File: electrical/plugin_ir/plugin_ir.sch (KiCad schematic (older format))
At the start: 2 parts, among them Q2 AO3400

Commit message: Merge from master
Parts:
- renumbered Q2 to Q?, R4 to R?
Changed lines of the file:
@@
 EESchema Schematic File Version 4
-LIBS:rasbot-cache
 EELAYER 29 0
 EELAYER END
 $Descr A4 11693 8268
 encoding utf-8
-Sheet 4 14
+Sheet 1 8
 Title ""
 Date ""
@@
 IR_OUT6
 $Comp
-L power:GND #PWR031
+L power:GND #PWR?
 U 1 1 5D41F6C3
 P 5300 7250
-F 0 "#PWR031" H 5300 7000 50  0001 C CNN
+F 0 "#PWR?" H 5300 7000 50  0001 C CNN
 F 1 "GND" H 5305 7077 50  0000 C CNN
 F 2 "" H 5300 7250 50  0001 C CNN
@@
 	5300 6750 5300 6700
 $Comp
-L Device:R R4
+L Device:R R?
 U 1 1 5D3ABC64
 P 5850 6950
-F 0 "R4" H 5920 6996 50  0000 L CNN
+F 0 "R?" H 5920 6996 50  0000 L CNN
 F 1 "0" H 5920 6905 50  0000 L CNN
 F 2 "Resistor_SMD:R_0805_2012Metric" V 5780 6950 50  0001 C CNN
@@
 	4950 1000 4950 6150
 $Comp
-L rasbot:AO3400 Q2
+L rasbot:AO3400 Q?
 U 1 1 5D3E0C2F
 P 5150 6950
-F 0 "Q2" H 5406 6996 50  0000 L CNN
+F 0 "Q?" H 5406 6996 50  0000 L CNN
 F 1 "AO3400" H 5406 6905 50  0000 L CNN
 F 2 "Package_TO_SOT_SMD:SOT-23" H 5975 6875 50  0001 C CNN

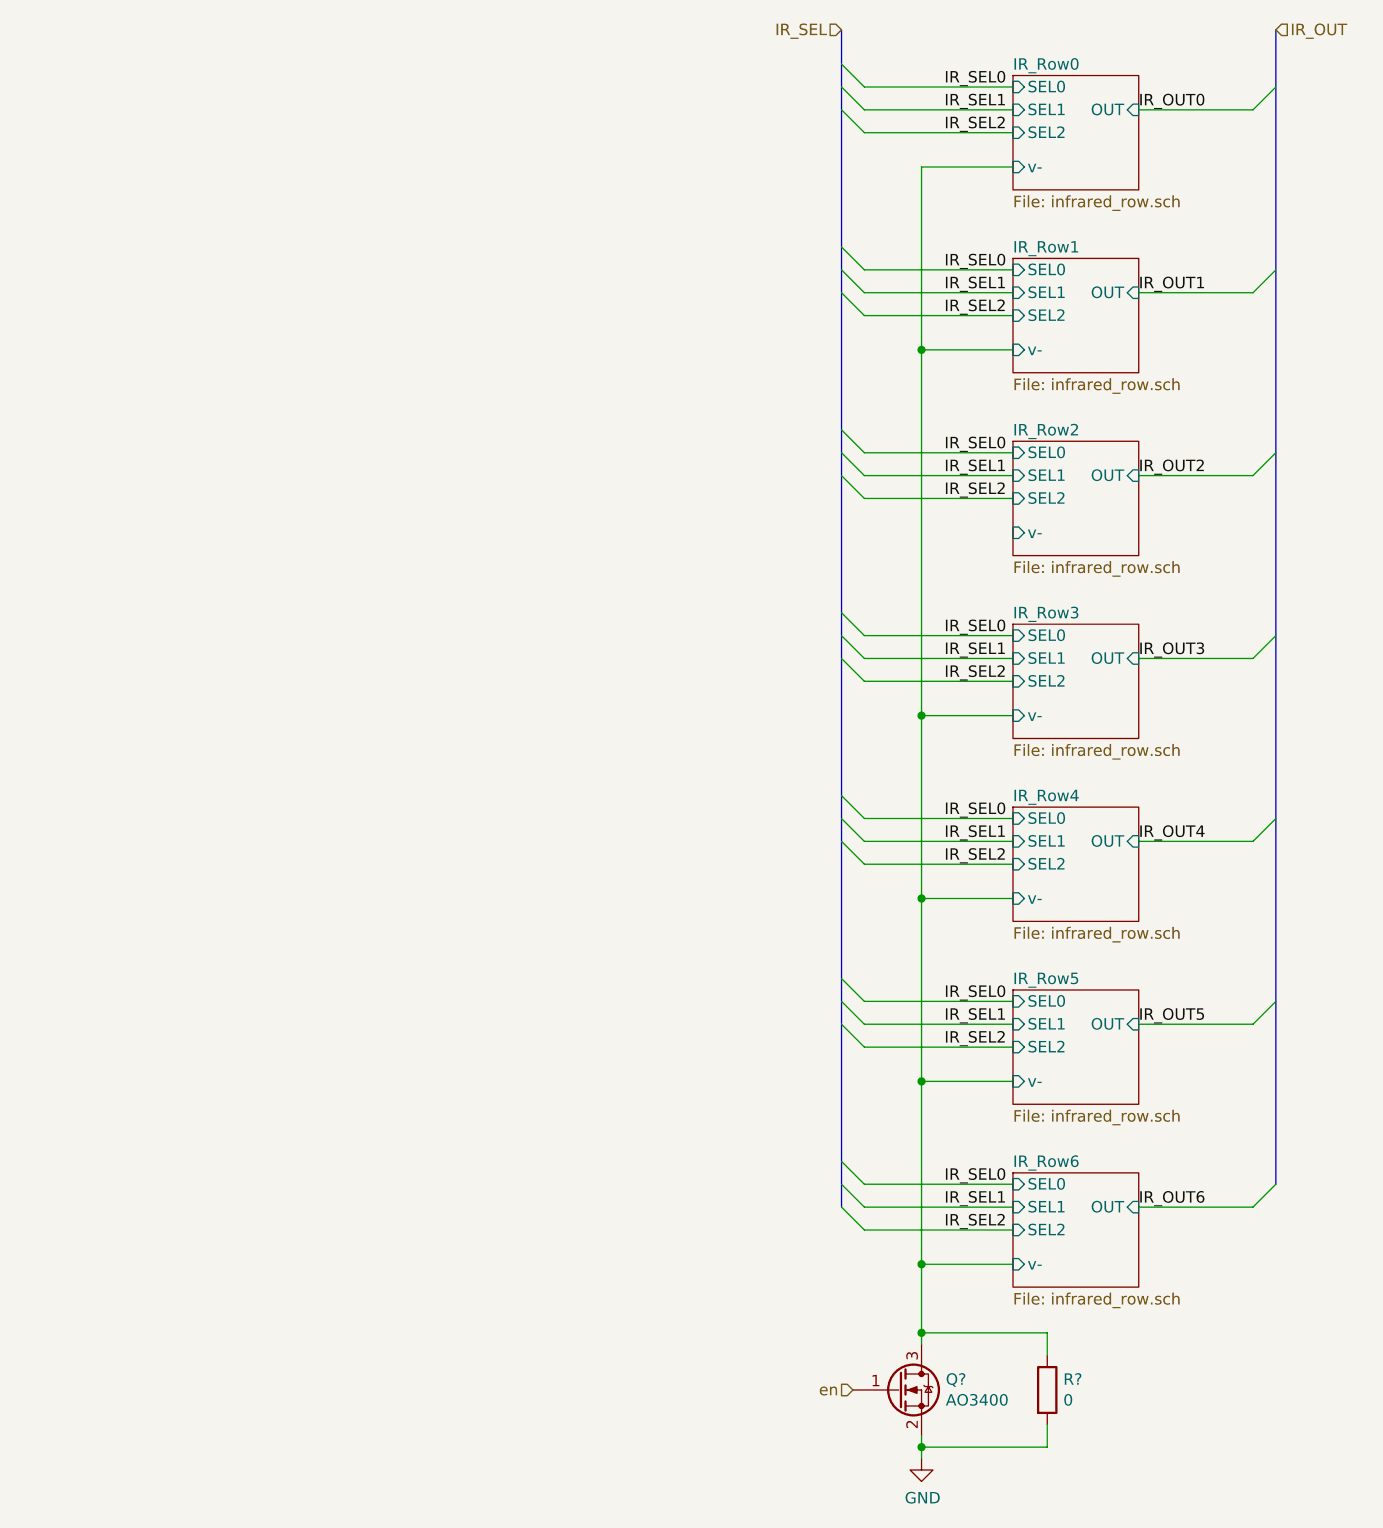
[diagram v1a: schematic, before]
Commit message: Give Up SEPIC and 9V LDO design
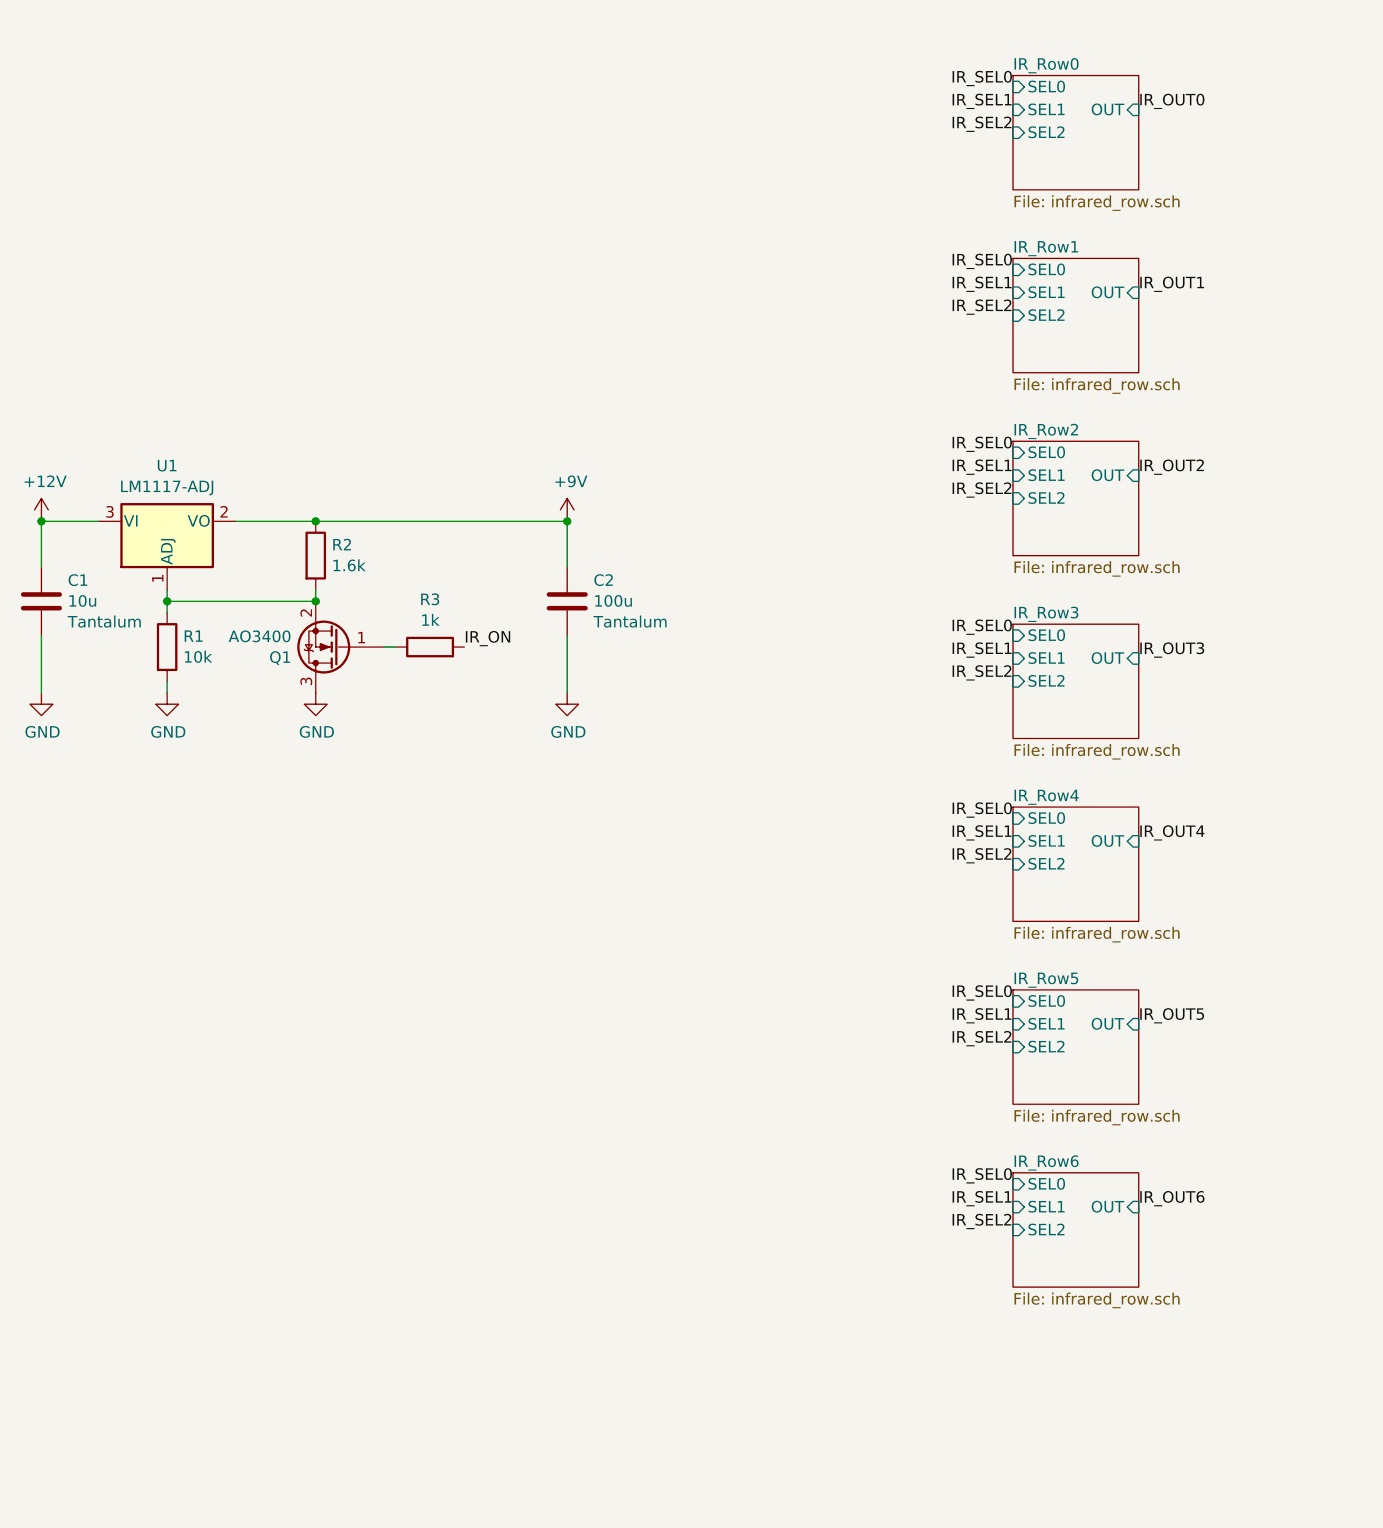
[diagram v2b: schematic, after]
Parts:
- removed R?: 0, Resistor_SMD:R_0805_2012Metric, symbol Device:R
- added C1: 10u, symbol Device:C
- added C2: 100u, symbol Device:C
- added R1: 10k, symbol Device:R
- added R2: 1.6k, symbol Device:R
- added R3: 1k, symbol Device:R
- added U1: LM1117-ADJ, symbol Regulator_Linear:LM1117-ADJ
- gave numbers to parts that had none: 1
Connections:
- net IR_Row0/v- is gone; now on net GND: Q1.3 (D)
- net GND: now also C1.2, C2.2, R1.2; no longer Q1.2 (S)
- net en: no longer names the net of Q1.1 (G)
- net en: now also R3.1
- new net: Q1.2 (S), R1.1, R2.2, U1.1 (ADJ)
- new net +12V: C1.1, U1.3 (VI)
- new net +9V: C2.1, R2.1, U1.2 (VO)
- new net IR_ON: R3.2
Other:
- moved on the sheet: Q1
